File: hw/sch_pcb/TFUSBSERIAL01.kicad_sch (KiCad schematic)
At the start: 29 parts, among them J1 USBC_USB4105-GF-A, J2 SM06B-GHS-TB, J3 SM06B-GHS-TB, M1 HOLE_TF, M2 HOLE_TF, M3 HOLE_TF, M4 HOLE_TF, M5 HOLE_TF, M6 HOLE_TF, U1 USBLC6-2SC6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

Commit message: Edit schema
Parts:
- added R10, R11, R8, R9: 100R, Resistor_SMD:R_0603_1608Metric, symbol Device:R
- added TP1: #DTR, symbol Connector:TestPoint
- added TP2: #DSR, symbol Connector:TestPoint
- added TP3: #DCD, symbol Connector:TestPoint
- added TP4: #RI, symbol Connector:TestPoint
- D2: UST_ID 5c70984412875079b91f8896 -> 60d581db1287500165f859a2
- D3, D4: UST_ID 5c70984412875079b91f8895 -> 60d582331287500165f859d0
- F1: value 750mA -> 350mA
- R5: value 270R -> 290R; UST_ID 5c70984512875079b91f8983 -> (none)
- R6, R7: value 270R -> 140R; UST_ID 5c70984512875079b91f8983 -> (none)
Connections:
- net #CTS: now also R11.2; no longer U2.6 (~{CTS})
- net #RTS: now also R10.2; no longer U2.19 (~{RTS})
- net +5V: now also C3.1, F1.2, FB1.2; no longer D1.1 (K), J2.1, J3.1
- net RXD: now also R9.2; no longer U2.1 (RXD)
- net TXD: now also R8.2; no longer U2.17 (TXD)
- net VBUS: now also C1.1, FB1.1; no longer F1.1
- net at U2.18 (~{DTR}): now also TP1.1
- net at U2.2 (~{RI}): now also TP4.1
- net at U2.4 (~{DSR}): now also TP2.1
- net at U2.5 (~{DCD}): now also TP3.1
- new net: R9.1, U2.1 (RXD)
- new net: D1.2 (A), F1.1, J2.1
- new net: R10.1, U2.19 (~{RTS})
- new net: R8.1, U2.17 (TXD)
- new net: D1.1 (K), J3.1
- new net: R11.1, U2.6 (~{CTS})
- no-connect marks 8 -> 4
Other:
- note removed: "Budou tu LED?"
- moved on the sheet: C1, C3, D1, F1, FB1, J2, J3

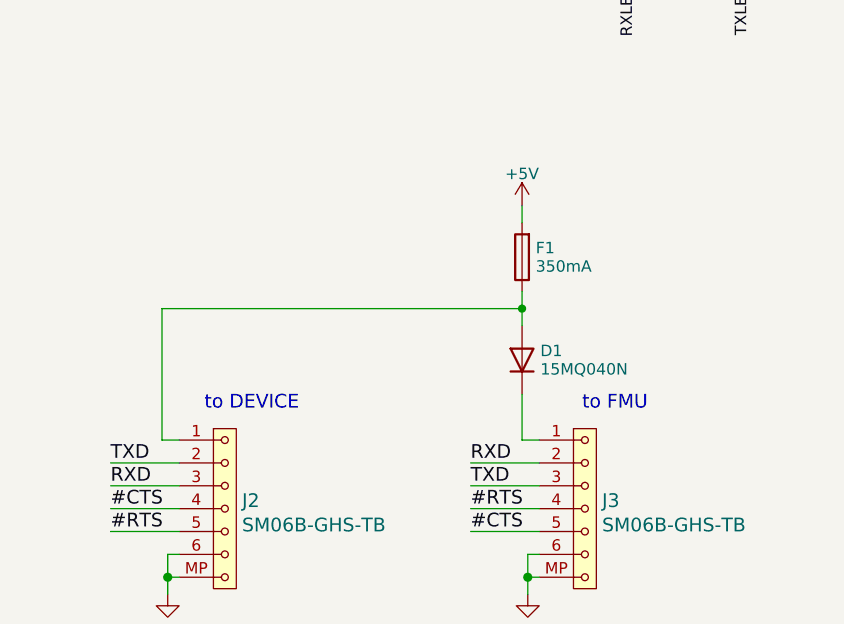
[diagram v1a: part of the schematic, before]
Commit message: Change fuse schematics symbol to polyfuse Solve some offgrid placed componets Rename Device connector to peripheral connector.
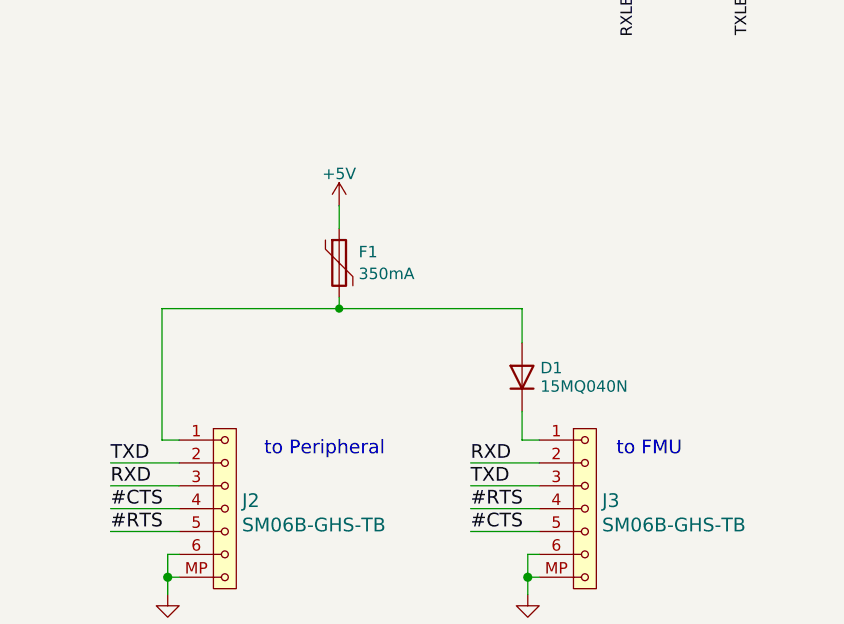
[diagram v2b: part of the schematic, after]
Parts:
- removed F1: 350mA, Mlab_F:1812, symbol Device:Fuse
- added F1: 350mA, symbol Device:Polyfuse
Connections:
- net +5V: now also F1.1
- net at D1.2 (A), J2.1: now also F1.2
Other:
- note added: "to Peripheral"
- note removed: "to DEVICE"
- moved on the sheet: D1
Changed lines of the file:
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@@
   (junction (at 95.25 109.22) (diameter 1.016) (color 0 0 0 0)
   )
-  (junction (at 247.65 110.49) (diameter 0) (color 0 0 0 0)
-  )
   (junction (at 138.43 66.04) (diameter 1.016) (color 0 0 0 0)
+  )
+  (junction (at 227.33 110.49) (diameter 0) (color 0 0 0 0)
   )
   (no_connect (at 43.815 49.53))
@@
     (stroke (width 0) (type solid))
   )
+  (wire (pts (xy 227.33 109.22) (xy 227.33 110.49))
+    (stroke (width 0) (type default))
+  )
   (wire (pts (xy 95.25 95.25) (xy 95.25 99.06))
     (stroke (width 0) (type default))
   )
+  (wire (pts (xy 227.33 110.49) (xy 247.65 110.49))
+    (stroke (width 0) (type default))
+  )
   (wire (pts (xy 138.43 66.04) (xy 138.43 86.36))
     (stroke (width 0) (type solid))
@@
     (stroke (width 0) (type default))
   )
-  (wire (pts (xy 247.65 99.06) (xy 247.65 100.965))
+  (wire (pts (xy 227.33 99.06) (xy 227.33 101.6))
     (stroke (width 0) (type default))
   )
@@
     (stroke (width 0) (type solid))
   )
-  (wire (pts (xy 207.645 110.49) (xy 247.65 110.49))
+  (wire (pts (xy 207.645 110.49) (xy 227.33 110.49))
     (stroke (width 0) (type default))
   )
@@
     (stroke (width 0) (type solid))
   )
-  (wire (pts (xy 247.65 110.49) (xy 247.65 112.395))
+  (wire (pts (xy 247.65 110.49) (xy 247.65 114.3))
     (stroke (width 0) (type default))
   )
@@
     (stroke (width 0) (type solid))
   )
-  (wire (pts (xy 247.65 108.585) (xy 247.65 110.49))
-    (stroke (width 0) (type default))
-  )
   (wire (pts (xy 260.35 55.245) (xy 260.35 57.785))
     (stroke (width 0) (type solid))
@@
     (stroke (width 0) (type solid))
   )
-  (wire (pts (xy 247.65 120.015) (xy 247.65 125.095))
+  (wire (pts (xy 247.65 121.92) (xy 247.65 125.095))
     (stroke (width 0) (type solid))
   )
@@
     (stroke (width 0) (type solid))
   )
-  (text "to DEVICE" (at 222.885 121.92 0)
+  (text "to Peripheral" (at 232.41 127 0)
     (effects (font (size 1.524 1.524)) (justify right bottom))
   )
-  (text "to FMU" (at 261.62 121.92 0)
+  (text "to FMU" (at 265.43 127 0)
     (effects (font (size 1.524 1.524)) (justify right bottom))
   )
@@
     )
   )
-  (symbol (lib_id "power:+5V") (at 247.65 99.06 0) (unit 1)
+  (symbol (lib_id "power:+5V") (at 227.33 99.06 0) (unit 1)
     (in_bom yes) (on_board yes) (dnp no) (fields_autoplaced)
-    (property "Reference" "#PWR0106" (at 247.65 102.87 0)
-      (effects (font (size 1.27 1.27)) hide)
-    )
-    (property "Value" "+5V" (at 247.65 95.5126 0)
-      (effects (font (size 1.27 1.27)))
-    )
-    (property "Footprint" "" (at 247.65 99.06 0)
-      (effects (font (size 1.27 1.27)) hide)
-    )
-    (property "Datasheet" "" (at 247.65 99.06 0)
+    (property "Reference" "#PWR0106" (at 227.33 102.87 0)
+      (effects (font (size 1.27 1.27)) hide)
+    )
+    (property "Value" "+5V" (at 227.33 95.5126 0)
+      (effects (font (size 1.27 1.27)))
+    )
+    (property "Footprint" "" (at 227.33 99.06 0)
+      (effects (font (size 1.27 1.27)) hide)
+    )
+    (property "Datasheet" "" (at 227.33 99.06 0)
       (effects (font (size 1.27 1.27)) hide)
     )
@@
         (path "/2bba972d-fb08-481b-94d3-048811539baf"
           (reference "D4") (unit 1)
+        )
+      )
+    )
+  )
+  (symbol (lib_id "Device:Polyfuse") (at 227.33 105.41 0) (unit 1)
+    (in_bom yes) (on_board yes) (dnp no) (fields_autoplaced)
+    (property "Reference" "F1" (at 229.489 104.1979 0)
+      (effects (font (size 1.27 1.27)) (justify left))
+    )
+    (property "Value" "350mA" (at 229.489 106.6221 0)
+      (effects (font (size 1.27 1.27)) (justify left))
+    )
+    (property "Footprint" "" (at 228.6 110.49 0)
+      (effects (font (size 1.27 1.27)) (justify left) hide)
+    )
+    (property "Datasheet" "~" (at 227.33 105.41 0)
+      (effects (font (size 1.27 1.27)) hide)
+    )
+    (pin "1")
+    (pin "2")
+    (instances
+      (project "TFUSBSERIAL01"
+        (path "/2bba972d-fb08-481b-94d3-048811539baf"
+          (reference "F1") (unit 1)
         )
       )
@@
     )
   )
-  (symbol (lib_id "Device:D") (at 247.65 116.205 90) (unit 1)
+  (symbol (lib_id "Device:D") (at 247.65 118.11 90) (unit 1)
     (in_bom yes) (on_board yes) (dnp no) (fields_autoplaced)
-    (property "Reference" "D1" (at 249.682 115.181 90)
+    (property "Reference" "D1" (at 249.682 117.086 90)
       (effects (font (size 1.27 1.27)) (justify right))
     )
-    (property "Value" "15MQ040N" (at 249.682 117.229 90)
+    (property "Value" "15MQ040N" (at 249.682 119.134 90)
       (effects (font (size 1.27 1.27)) (justify right))
     )
-    (property "Footprint" "Diode_SMD:D_SMA" (at 247.65 116.205 0)
-      (effects (font (size 1.27 1.27)) hide)
-    )
-    (property "Datasheet" "~" (at 247.65 116.205 0)
+    (property "Footprint" "Diode_SMD:D_SMA" (at 247.65 118.11 0)
+      (effects (font (size 1.27 1.27)) hide)
+    )
+    (property "Datasheet" "~" (at 247.65 118.11 0)
       (effects (font (size 1.27 1.27)) hide)
     )
@@
         )
       )
-    )
-  )
-  (symbol (lib_id "Device:Fuse") (at 247.65 104.775 180) (unit 1)
-    (in_bom yes) (on_board yes) (dnp no) (fields_autoplaced)
-    (property "Reference" "F1" (at 249.174 103.751 0)
-      (effects (font (size 1.27 1.27)) (justify right))
-    )
-    (property "Value" "350mA" (at 249.174 105.799 0)
-      (effects (font (size 1.27 1.27)) (justify right))
-    )
-    (property "Footprint" "Mlab_F:1812" (at 249.428 104.775 90)
-      (effects (font (size 1.27 1.27)) hide)
-    )
-    (property "Datasheet" "~" (at 247.65 104.775 0)
-      (effects (font (size 1.27 1.27)) hide)
-    )
-    (pin "1")
-    (pin "2")
-    (instances
-      (project "TFUSBSERIAL01"
-        (path "/2bba972d-fb08-481b-94d3-048811539baf"
-          (reference "F1") (unit 1)
-        )
-      )

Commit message: usb serial
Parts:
- added FID1, FID2: Fiducial, Fiducial:Fiducial_1mm_Mask2mm, symbol Mechanical:Fiducial
- F1: footprint (none) -> Fuse:Fuse_0805_2012Metric
- TP1, TP2, TP3, TP4: footprint (none) -> TestPoint:TestPoint_Pad_D1.0mm
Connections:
- net GND: now also C5.2; no longer C5.1
- net at C2.1, U2.10 (3V3OUT), U2.20 (VCCIO): now also C5.1; no longer C5.2
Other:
- company: Mlab www.mlab.cz -> www.thunderfly.cz
- title: NAME -> TFUSBSERIAL01A
- moved on the sheet: C5, J1, R1, R2, U1

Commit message: update ust_id
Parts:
- D1: UST_ID (none) -> 5c70984512875079b91f88b0
- F1: UST_ID (none) -> 650b8191462c6d9e7205477b
- J2, J3: UST_ID (none) -> 5fa0f70212875025b3977932
- R10, R11, R8, R9: UST_ID (none) -> 5c70984512875079b91f8956
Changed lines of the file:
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@@
       (effects (font (size 1.27 1.27)) hide)
     )
-    (property "UST_ID" "" (at 165.735 96.52 0)
+    (property "UST_ID" "5c70984512875079b91f8956" (at 165.735 96.52 0)
       (effects (font (size 1.27 1.27)) hide)
     )
@@
     (property "Datasheet" "" (at 214.63 125.095 0)
       (effects (font (size 1.524 1.524)))
+    )
+    (property "UST_ID" "5fa0f70212875025b3977932" (at 214.63 132.715 0)
+      (effects (font (size 1.27 1.27)) hide)
     )
     (pin "1")
@@
       (effects (font (size 1.27 1.27)) hide)
     )
+    (property "UST_ID" "650b8191462c6d9e7205477b" (at 227.33 105.41 0)
+      (effects (font (size 1.27 1.27)) hide)
+    )
     (pin "1")
     (pin "2")
@@
       (effects (font (size 1.27 1.27)) hide)
     )
-    (property "UST_ID" "" (at 165.735 99.06 0)
+    (property "UST_ID" "5c70984512875079b91f8956" (at 165.735 99.06 0)
       (effects (font (size 1.27 1.27)) hide)
     )
@@
       (effects (font (size 1.27 1.27)) hide)
     )
-    (property "UST_ID" "" (at 165.735 93.98 0)
+    (property "UST_ID" "5c70984512875079b91f8956" (at 165.735 93.98 0)
       (effects (font (size 1.27 1.27)) hide)
     )
@@
     (property "Datasheet" "" (at 254.635 125.095 0)
       (effects (font (size 1.524 1.524)))
+    )
+    (property "UST_ID" "5fa0f70212875025b3977932" (at 254.635 132.715 0)
+      (effects (font (size 1.27 1.27)) hide)
     )
     (pin "1")
@@
       (effects (font (size 1.27 1.27)) hide)
     )
-    (property "UST_ID" "" (at 165.735 101.6 0)
+    (property "UST_ID" "5c70984512875079b91f8956" (at 165.735 101.6 0)
       (effects (font (size 1.27 1.27)) hide)
     )
@@
       (effects (font (size 1.27 1.27)) hide)
     )
+    (property "UST_ID" "5c70984512875079b91f88b0" (at 247.65 118.11 0)
+      (effects (font (size 1.27 1.27)) hide)
+    )

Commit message: layout updates
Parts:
- C1: UST_ID 5c70984712875079b91f8b49 -> 5c70984812875079b91f8bef
- C2, C4, C5: UST_ID 5c70984712875079b91f8b4c -> 5c70984812875079b91f8bf2
- C3: UST_ID 5c70984812875079b91f8bbd -> 5c70984812875079b91f8bf5
- FID1, FID2: footprint Fiducial:Fiducial_1mm_Mask2mm -> Fiducial:Fiducial_0.5mm_Mask1mm
- R1, R2: UST_ID 5fa0fc3e12875025b3977997 -> 628d1404dc56076e9a223650
- R3: UST_ID 5c70984612875079b91f8995 -> 5c70984512875079b91f8960
- R4: UST_ID 5c70984612875079b91f899f -> 5c70984512875079b91f8962
- R5: value 290R -> 287R; UST_ID (none) -> 5c70984512875079b91f8969
- R6, R7: value 140R -> 130R; UST_ID (none) -> 5cd08b17128750448e4542b1
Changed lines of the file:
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@@
       (effects (font (size 1.27 1.27)) hide)
     )
-    (property "UST_ID" "5c70984612875079b91f899f" (at 95.25 115.57 0)
+    (property "UST_ID" "5c70984512875079b91f8962" (at 95.25 115.57 0)
       (effects (font (size 1.27 1.27)) hide)
     )
@@
       (effects (font (size 1.27 1.27)) (justify left))
     )
-    (property "Value" "140R" (at 274.828 62.744 0)
+    (property "Value" "130R" (at 274.828 62.744 0)
       (effects (font (size 1.27 1.27)) (justify left))
     )
@@
       (effects (font (size 1.27 1.27)) hide)
     )
-    (property "UST_ID" "" (at 273.05 61.595 0)
+    (property "UST_ID" "5cd08b17128750448e4542b1" (at 273.05 61.595 0)
       (effects (font (size 1.27 1.27)) hide)
     )
@@
       (effects (font (size 1.27 1.27)) hide)
     )
-    (property "UST_ID" "5c70984712875079b91f8b4c" (at 149.86 82.55 0)
+    (property "UST_ID" "5c70984812875079b91f8bf2" (at 149.86 82.55 0)
       (effects (font (size 1.27 1.27)) hide)
     )
@@
       (effects (font (size 1.27 1.27)) (justify left))
     )
-    (property "Value" "290R" (at 262.128 62.744 0)
+    (property "Value" "287R" (at 262.128 62.744 0)
       (effects (font (size 1.27 1.27)) (justify left))
     )
@@
       (effects (font (size 1.27 1.27)) hide)
     )
-    (property "UST_ID" "" (at 260.35 61.595 0)
+    (property "UST_ID" "5c70984512875079b91f8969" (at 260.35 61.595 0)
       (effects (font (size 1.27 1.27)) hide)
     )
@@
       (effects (font (size 1.27 1.27)) (justify left))
     )
-    (property "Value" "140R" (at 248.793 62.744 0)
+    (property "Value" "130R" (at 248.793 62.744 0)
       (effects (font (size 1.27 1.27)) (justify left))
     )
@@
       (effects (font (size 1.27 1.27)) hide)
     )
-    (property "UST_ID" "" (at 247.015 61.595 0)
+    (property "UST_ID" "5cd08b17128750448e4542b1" (at 247.015 61.595 0)
       (effects (font (size 1.27 1.27)) hide)
     )
@@
       (effects (font (size 1.27 1.27)) hide)
     )
-    (property "UST_ID" "5fa0fc3e12875025b3977997" (at 59.69 66.04 0)
+    (property "UST_ID" "628d1404dc56076e9a223650" (at 59.69 66.04 0)
       (effects (font (size 1.27 1.27)) hide)
     )
@@
       (effects (font (size 1.27 1.27)) hide)
     )
-    (property "UST_ID" "5fa0fc3e12875025b3977997" (at 59.69 68.58 0)
+    (property "UST_ID" "628d1404dc56076e9a223650" (at 59.69 68.58 0)
       (effects (font (size 1.27 1.27)) hide)
     )
@@
       (effects (font (size 1.27 1.27)) (justify left))
     )
-    (property "Footprint" "Fiducial:Fiducial_1mm_Mask2mm" (at 227.33 16.51 0)
+    (property "Footprint" "Fiducial:Fiducial_0.5mm_Mask1mm" (at 227.33 16.51 0)
       (effects (font (size 1.27 1.27)) hide)
     )
@@
       (effects (font (size 1.27 1.27)) hide)
     )
-    (property "UST_ID" "5c70984712875079b91f8b4c" (at 106.68 97.79 0)
+    (property "UST_ID" "5c70984812875079b91f8bf2" (at 106.68 97.79 0)
       (effects (font (size 1.27 1.27)) hide)
     )
@@
       (effects (font (size 1.27 1.27)) hide)
     )
-    (property "UST_ID" "5c70984712875079b91f8b49" (at 88.265 71.12 0)
+    (property "UST_ID" "5c70984812875079b91f8bef" (at 88.265 71.12 0)
       (effects (font (size 1.27 1.27)) hide)
     )
@@
       (effects (font (size 1.27 1.27)) hide)
     )
-    (property "UST_ID" "5c70984712875079b91f8b4c" (at 128.905 71.12 0)
+    (property "UST_ID" "5c70984812875079b91f8bf2" (at 128.905 71.12 0)
       (effects (font (size 1.27 1.27)) hide)
     )
@@
       (effects (font (size 1.27 1.27)) hide)
     )
-    (property "UST_ID" "5c70984612875079b91f8995" (at 95.25 102.87 0)
+    (property "UST_ID" "5c70984512875079b91f8960" (at 95.25 102.87 0)
       (effects (font (size 1.27 1.27)) hide)
     )
@@
       (effects (font (size 1.27 1.27)) (justify left))
     )
-    (property "Footprint" "Fiducial:Fiducial_1mm_Mask2mm" (at 227.33 22.86 0)
+    (property "Footprint" "Fiducial:Fiducial_0.5mm_Mask1mm" (at 227.33 22.86 0)
       (effects (font (size 1.27 1.27)) hide)
     )
@@
       (effects (font (size 1.27 1.27)) hide)
     )
-    (property "UST_ID" "5c70984812875079b91f8bbd" (at 107.315 71.12 0)
-      (effects (font (size 1.27 1.27)) hide)
-    )
+    (property "UST_ID" "5c70984812875079b91f8bf5" (at 107.315 71.12 0)
+      (effects (font (size 1.27 1.27)) hide)
+    )

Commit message: Kontrola a upravy pred vyrobou.
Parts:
- D1: value 15MQ040N -> SRL23; footprint Diode_SMD:D_SMA -> Diode_SMD:D_SOD-323_HandSoldering; UST_ID 5c70984512875079b91f88b0 -> 651003fd462c6d9e72054b2f
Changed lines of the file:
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@@
       (effects (font (size 1.27 1.27)) (justify right))
     )
-    (property "Value" "15MQ040N" (at 249.682 119.134 90)
+    (property "Value" "SRL23" (at 249.682 119.134 90)
       (effects (font (size 1.27 1.27)) (justify right))
     )
-    (property "Footprint" "Diode_SMD:D_SMA" (at 247.65 118.11 0)
+    (property "Footprint" "Diode_SMD:D_SOD-323_HandSoldering" (at 247.65 118.11 0)
       (effects (font (size 1.27 1.27)) hide)
     )
@@
       (effects (font (size 1.27 1.27)) hide)
     )
-    (property "UST_ID" "5c70984512875079b91f88b0" (at 247.65 118.11 0)
+    (property "UST_ID" "651003fd462c6d9e72054b2f" (at 247.65 118.11 0)
       (effects (font (size 1.27 1.27)) hide)
     )
